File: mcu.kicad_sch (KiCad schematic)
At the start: 21 parts, among them J1 TC2030, J2 Conn_01x03_Pin, J4 Conn_02x07_Odd_Even, J5 Conn_01x05_Pin, J9 Conn_01x08_Pin, U1 STM32U031K8Ux, Y1 G83270025

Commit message: Change of concept - one board, not multiple
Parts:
- removed J4: Conn_02x07_Odd_Even, Connector_PinHeader_2.54mm:PinHeader_2x07_P2.54mm_Vertical, symbol Connector_Generic:Conn_02x07_Odd_Even
- removed J5: Conn_01x05_Pin, Connector_PinHeader_2.54mm:PinHeader_1x05_P2.54mm_Vertical, symbol Connector:Conn_01x05_Pin
- added R10, R11, R3, R6, R7, R8, R9: 0R, Resistor_SMD:R_0603_1608Metric, symbol Device:R_Small
- renumbered J9 to J3, R33 to R1, R4 to R12, R5 to R13, R1 to R2, R2 to R4, R3 to R5
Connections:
- net +3V3: now also R10.2, R3.2; no longer J3.1 (Pin_1), J3.6 (Pin_6)
- net GND: now also R6.2, R9.2; no longer J3.2 (Pin_2), J3.5 (Pin_5)
- net I2C_SCL: now also R7.2; no longer J3.3 (Pin_3)
- net I2C_SDA: now also R8.2; no longer J3.4 (Pin_4)
- net PWR_WKUP: now also R11.2; no longer J3.7 (Pin_7)
- new net: J3.1 (Pin_1), R3.1
- new net: J3.2 (Pin_2), R6.1
- new net: J3.3 (Pin_3), R7.1
- new net: J3.7 (Pin_7), R11.1
- new net: J3.5 (Pin_5), R9.1
- new net: J3.4 (Pin_4), R8.1
- new net: J3.6 (Pin_6), R10.1
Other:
- moved on the sheet: J3, R12, R13

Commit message: Early pcb project
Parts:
- J3: footprint (none) -> Connector_PinHeader_2.54mm:PinHeader_1x08_P2.54mm_Vertical
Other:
- note added: "MCU"

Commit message: Finished pcb project
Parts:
- removed J3: Conn_01x08_Pin, Connector_PinHeader_2.54mm:PinHeader_1x08_P2.54mm_Vertical, symbol Connector:Conn_01x08_Pin
- removed R10, R11, R3, R4, R5, R6, R7, R8, R9: 0R, Resistor_SMD:R_0603_1608Metric, symbol Device:R_Small
- added JP1, JP2, JP3, JP4, JP5, JP6: SolderJumper_2_Open, Jumper:SolderJumper-2_P1.3mm_Open_TrianglePad1.0x1.5mm, symbol Jumper:SolderJumper_2_Open
- J2: footprint Connector_PinSocket_2.54mm:PinSocket_1x03_P2.54mm_Vertical -> Connector_JST:JST_GH_BM03B-GHS-TBT_1x03-1MP_P1.25mm_Vertical
- renumbered C6 to C2, C7 to C3, C2 to C4, C3 to C5, C5 to C6, C4 to C7, R2 to R1, R1 to R2, R12 to R3, R13 to R4
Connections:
- net I2C_SDL is gone; now on net I2C2_SCL: U1.13 (PA7)
- net POWER_MANAGEMENT_INTERRUPT is gone; now on net DIODE_TIM_CH: U1.11 (PA5)
- net +3V3: now also JP3.1 (A)
- net DIODE_TIM_CH: no longer U1.10 (PA4)
- net GND: now also JP4.1 (A)
- net PWR_WKUP: now also JP5.1 (A), JP6.1 (A)
- net I2C_SCL renamed I2C2_SCL
- net I2C2_SCL: now also JP1.1 (A)
- net I2C_SDA renamed I2C2_SDA
- net I2C2_SDA: now also JP2.1 (A)
- new net INT: U1.10 (PA4)
- new net INT1: JP5.2 (B)
- new net INT2: JP6.2 (B)
- new net SCL_A: JP1.2 (B)
- new net SDA_A: JP2.2 (B)
- new net SDO: JP3.2 (B), JP4.2 (B)
- no-connect marks 1 -> 0
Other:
- moved on the sheet: R3, R4

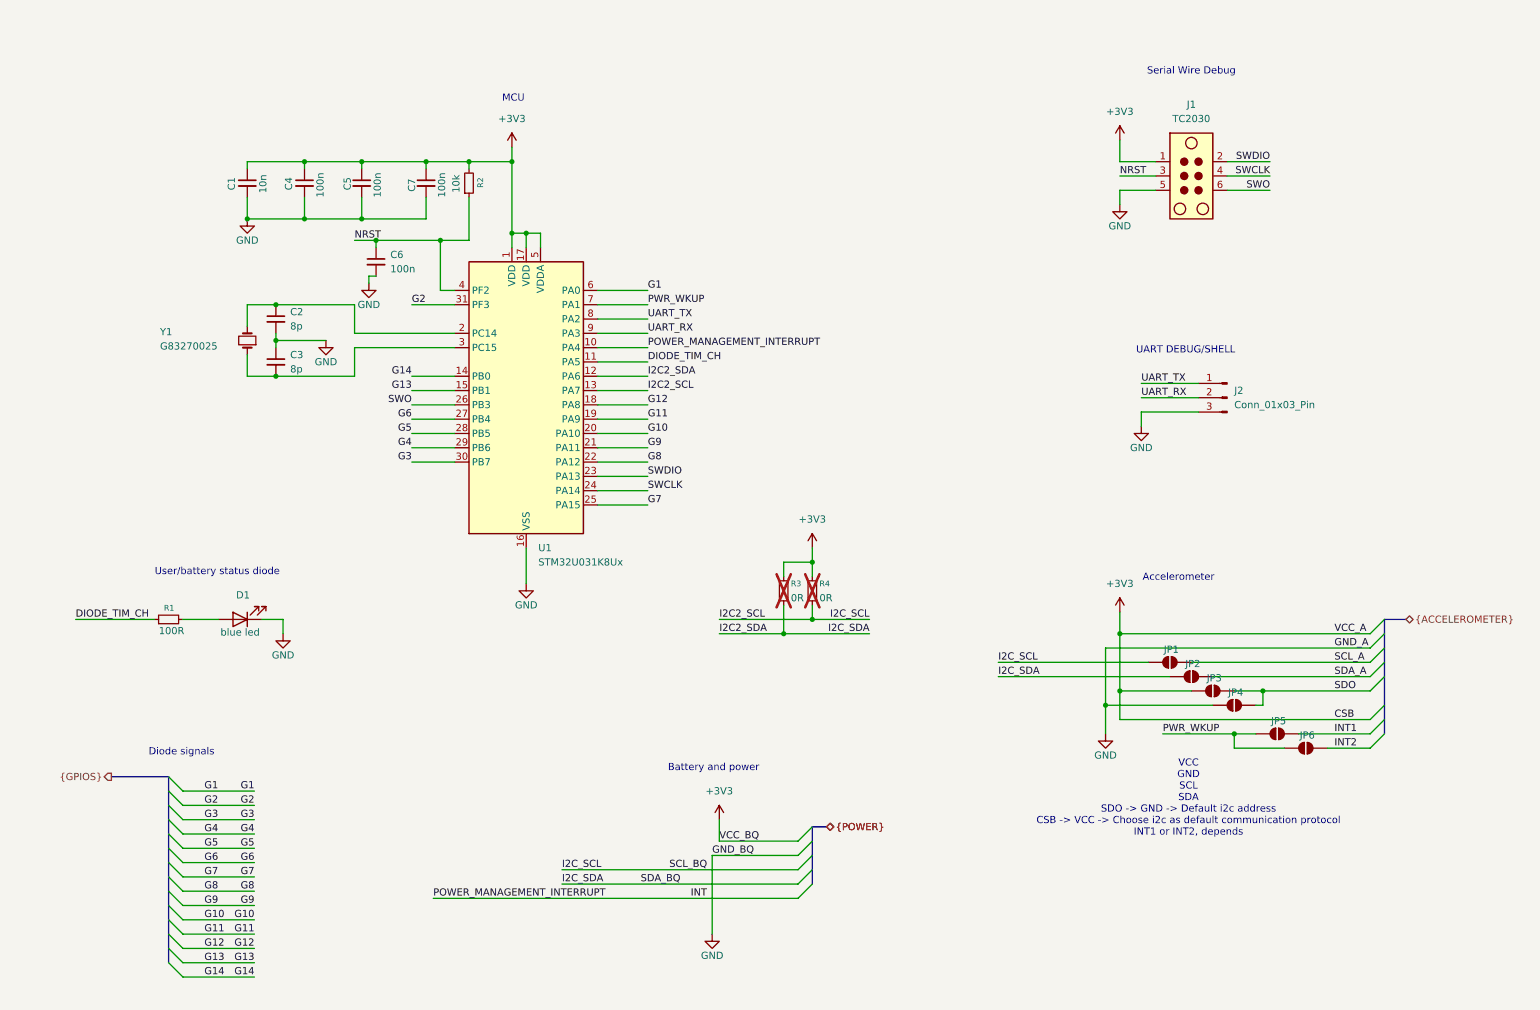
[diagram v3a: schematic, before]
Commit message: Add new mcu and better leds layout
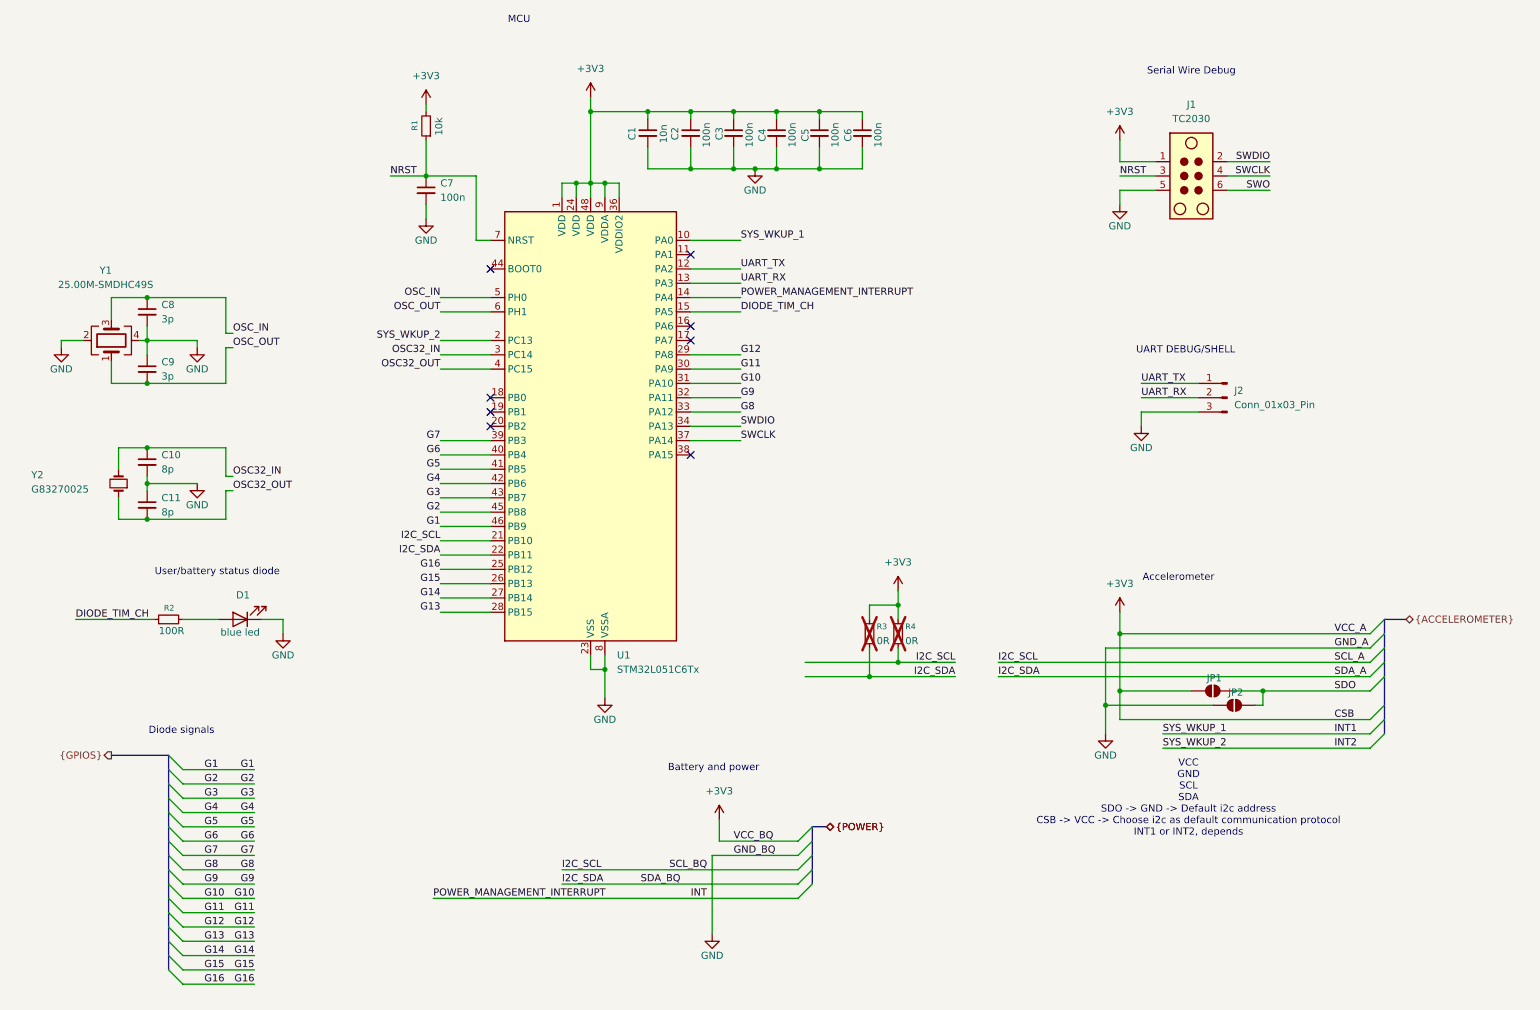
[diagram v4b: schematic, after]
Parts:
- removed JP1, JP2, JP5, JP6: SolderJumper_2_Open, Jumper:SolderJumper-2_P1.3mm_Open_TrianglePad1.0x1.5mm, symbol Jumper:SolderJumper_2_Open
- removed U1: STM32U031K8Ux, Package_DFN_QFN:QFN-32-1EP_5x5mm_P0.5mm_EP3.45x3.45mm, symbol MCU_ST_STM32U0:STM32U031K8Ux
- added C5, C6: 100n, Capacitor_SMD:C_0603_1608Metric, symbol Device:C_Small
- added C8, C9: 3p, Capacitor_SMD:C_0603_1608Metric, symbol Device:C_Small
- added U1: STM32L051C6Tx, Package_QFP:LQFP-48_7x7mm_P0.5mm, symbol MCU_ST_STM32L0:STM32L051C6Tx
- added Y1: 25.00M-SMDHC49S, Crystal:Crystal_SMD_3225-4Pin_3.2x2.5mm, symbol Device:Crystal_GND24
- renumbered C2 to C10, C3 to C11, C4 to C2, C5 to C3, C7 to C4, C6 to C7, JP3 to JP1, JP4 to JP2, R2 to R1, R1 to R2, Y1 to Y2
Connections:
- net +3V3: now also C5.1, C6.1, U1.1 (VDD), U1.24 (VDD), U1.36 (VDDIO2), U1.48 (VDD), U1.9 (VDDA)
- net DIODE_TIM_CH: now also U1.15 (PA5)
- net G1: now also U1.46 (PB9)
- net G10: now also U1.31 (PA10)
- net G11: now also U1.30 (PA9)
- net G12: now also U1.29 (PA8)
- net G13: now also U1.28 (PB15)
- net G14: now also U1.27 (PB14)
- net G2: now also U1.45 (PB8)
- net G3: now also U1.43 (PB7)
- net G4: now also U1.42 (PB6)
- net G5: now also U1.41 (PB5)
- net G6: now also U1.40 (PB4)
- net G7: now also U1.39 (PB3)
- net G8: now also U1.33 (PA12)
- net G9: now also U1.32 (PA11)
- net GND: now also C5.2, C6.2, C8.2, C9.1, U1.23 (VSS), U1.35 (VSS), U1.47 (VSS), U1.8 (VSSA), Y1.2, Y1.4
- net INT: now also U1.14 (PA4)
- net INT1: now also U1.10 (PA0)
- net INT2: now also U1.2 (PC13)
- net NRST: now also U1.7 (NRST)
- net SWCLK: now also U1.37 (PA14)
- net SWDIO: now also U1.34 (PA13)
- net UART_RX: now also U1.13 (PA3)
- net UART_TX: now also U1.12 (PA2)
- net OSC32_OUT: now reaches C11.2, Y2.1
- net OSC32_OUT: now also U1.4 (PC15)
- net OSC32_IN: now reaches C10.1, Y2.2
- net OSC32_IN: now also U1.3 (PC14)
- net I2C2_SCL renamed I2C_SCL
- net I2C_SCL: now also U1.21 (PB10)
- net I2C2_SDA renamed I2C_SDA
- net I2C_SDA: now also U1.22 (PB11)
- new net G15: U1.26 (PB13)
- new net G16: U1.25 (PB12)
- new net OSC_IN: C8.1, U1.5 (PH0), Y1.3
- new net OSC_OUT: C9.2, U1.6 (PH1), Y1.1
- no-connect marks 0 -> 8
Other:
- moved on the sheet: C1, C10, C11, C2, C3, C4, C7, R1, R3, R4, Y2

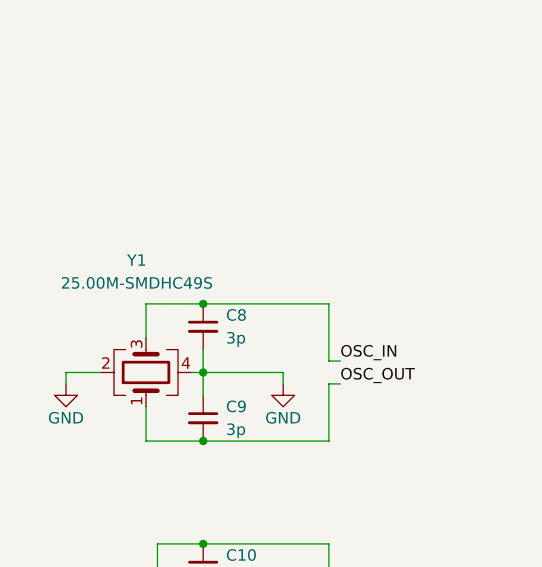
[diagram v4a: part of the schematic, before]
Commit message: Crystal resonator change
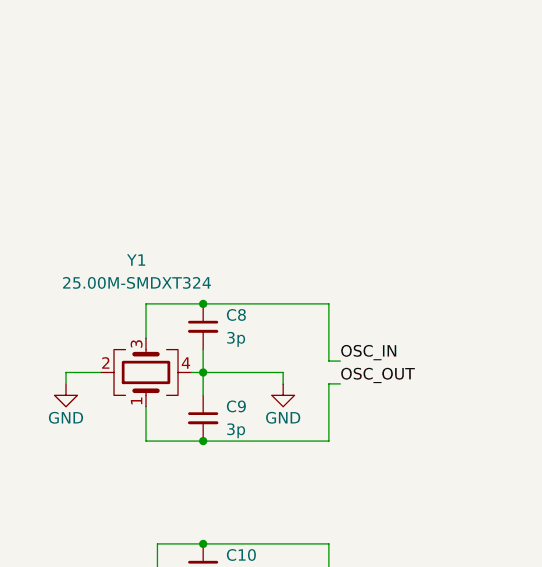
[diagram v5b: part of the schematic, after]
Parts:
- Y1: value 25.00M-SMDHC49S -> 25.00M-SMDXT324
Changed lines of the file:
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@@
 			)
 		)
-		(property "Value" "25.00M-SMDHC49S"
+		(property "Value" "25.00M-SMDXT324"
 			(at 32.004 65.024 90)
 			(effects
